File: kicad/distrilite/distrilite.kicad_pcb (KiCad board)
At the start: 2 copper layers, 49.5 x 128.3 mm, 28 parts, among them J1 Conn_01x03_Male, J10 Conn_01x03_Male, J11 Conn_01x03_Male, J12 Conn_01x03_Male, J13 LED_DOUT, J2 Conn_01x03_Male, J3 Conn_01x03_Male, J34 LED_DIN, J4 Conn_01x03_Male, J5 Conn_01x03_Male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

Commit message: ajout condo et validation ?
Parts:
- added C1: CP, Capacitors_ThroughHole:CP_Radial_D10.0mm_P3.80mm, F.Cu at (39.4, 149.1)
- added C2: CP, Capacitors_ThroughHole:CP_Radial_D10.0mm_P3.80mm, F.Cu at (52.8, 149.1)
- H1, H2, H3, H4: footprint Mounting_Holes:MountingHole_3.2mm_M3_Pad_Via -> Mounting_Holes:MountingHole_3.2mm_M3_Pad
- moved J1 31.2 mm to (35.8, 138.9)
- moved J11 31.2 mm to (35.8, 58.9)
- moved J12 31.2 mm to (56.1, 58.9)
- moved J2 31.2 mm to (56.1, 138.9)
- moved J5 31.2 mm to (35.8, 108.5)
- moved J6 31.2 mm to (56.1, 108.5)
- moved J7 31.2 mm to (35.8, 91.9)
- moved J8 31.2 mm to (56.1, 91.9)
- moved JP2 31.2 mm to (49.8, 116.1)
- moved REF** 31.2 mm to (59.9, 45.0)
- moved J13 31.2 mm to (38.4, 42.4)
- moved J3 31.2 mm to (35.8, 123.7)
- moved J9 31.2 mm to (35.8, 75.4)
- moved JP3 31.2 mm to (49.8, 99.6)
- moved JP4 31.2 mm to (49.8, 83.1)
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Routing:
- net GND: track 0.00 -> 165.4 mm
- net +12V: track 252.0 -> 271.2 mm
- net DATA_IN: track 12.2 -> 23.4 mm
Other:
- board size 49.5 x 128.3 mm -> 50.3 x 138.4 mm

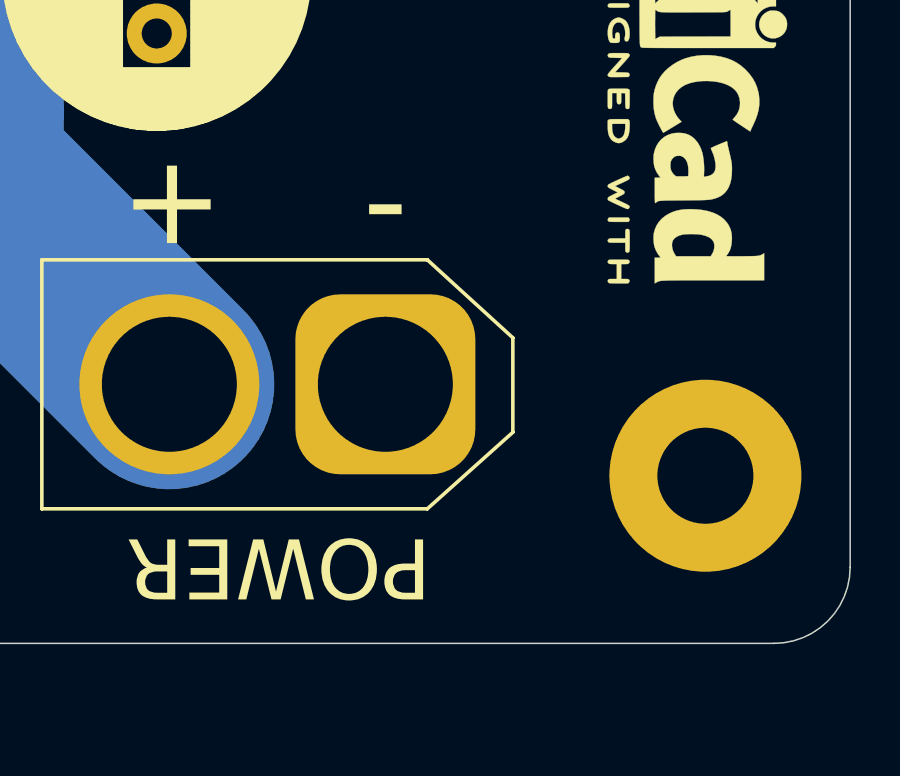
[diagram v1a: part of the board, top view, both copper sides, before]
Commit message: clearance et pad gnd
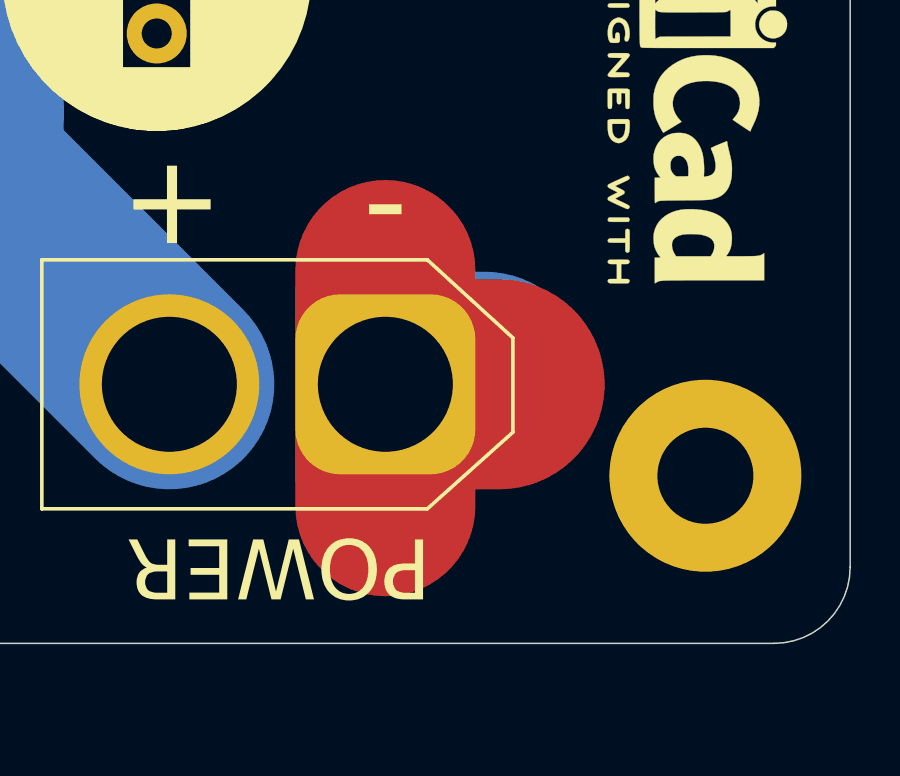
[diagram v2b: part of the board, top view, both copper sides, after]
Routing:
- net GND: track 165.4 -> 185.5 mm
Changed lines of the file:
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@@
     (thickness 1.6)
     (drawings 37)
-    (tracks 62)
+    (tracks 68)
     (zones 0)
     (modules 30)
@@
   (page A4)
   (layers
-    (0 F.Cu signal hide)
+    (0 F.Cu signal)
     (31 B.Cu signal)
     (32 B.Adhes user)
@@
   (segment (start 43.434 59.69) (end 43.434 56.642) (width 4) (layer B.Cu) (net 7))
   (segment (start 63.754 58.928) (end 63.754 138.938) (width 4) (layer B.Cu) (net 7))
+  (segment (start 60.452 161.492) (end 60.452 164.592) (width 6) (layer B.Cu) (net 7))
+  (segment (start 63.754 164.338) (end 60.96 164.338) (width 7) (layer B.Cu) (net 7))
+  (segment (start 60.452 164.592) (end 60.452 167.692) (width 6) (layer B.Cu) (net 7))
+  (segment (start 60.452 168.656) (end 60.452 164.592) (width 6) (layer F.Cu) (net 7))
+  (segment (start 60.452 160.782) (end 60.452 164.592) (width 6) (layer F.Cu) (net 7))
+  (segment (start 64.262 164.592) (end 60.96 164.592) (width 7) (layer F.Cu) (net 7))
   (segment (start 39.624 143.838) (end 39.624 138.938) (width 1) (layer F.Cu) (net 8))
   (segment (start 34.544 148.918) (end 34.544 160.194) (width 1) (layer F.Cu) (net 8))
